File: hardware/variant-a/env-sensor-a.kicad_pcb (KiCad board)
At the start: 4 copper layers, 30 x 34 mm, 64 parts, among them J1 USB-C 16P, J2 Molex PicoBlade 3P, Q1 2N7002, SW1 SW_PROV, U1 ESP32-C6-MINI-1-N4, U2 SHT45-AD1F, U3 TPS62840DLC, U4 BQ24074RGTR, U5 USBLC6-2SC6

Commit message: build(boardgen): regenerate local charger programming layout
Regenerate both variants from the local C9/R12/R13 placement and routing correction. Fresh reports retain A42/B34 incomplete development connectivity and zero errors, warnings or parity differences; these generated boards are not fabrication approval.
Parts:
- moved R20 26.6 mm to (128.9, 88.0), turned to 90 degrees
- moved R12 19.8 mm to (121.5, 67.2)
- moved R13 19.2 mm to (121.5, 70.3), turned to 270 degrees
- moved R18 9.42 mm to (120.2, 87.0)
- turned C9 to 180 degrees
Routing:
- net BTN_PROV: track 131.5 -> 20.5 mm, vias 9 -> 0
- net EN: track 81.1 -> 6.70 mm, vias 5 -> 0
- net UART_RX: track 16.3 -> 78.9 mm, vias 1 -> 5
- net CHG_N: track 7.20 -> 56.8 mm, vias 2 -> 4
- net UART_TX: track 38.9 -> 0.00 mm, vias 3 -> 0
- net USB_EN2: track 29.9 -> 46.1 mm, vias 2 -> 5
- net LED_A: track 12.6 -> 0.00 mm, vias 2 -> 0
- net PACK_TS: track 27.3 -> 17.7 mm
- net ISET: track 0.00 -> 4.09 mm
- net ITERM: track 0.00 -> 3.99 mm
- net VBAT: track 15.3 -> 17.7 mm
- net GND: track 43.3 -> 45.4 mm, vias 20 -> 24
- net VBUS: track 11.3 -> 9.80 mm
- net ILIM: track 21.5 -> 22.3 mm

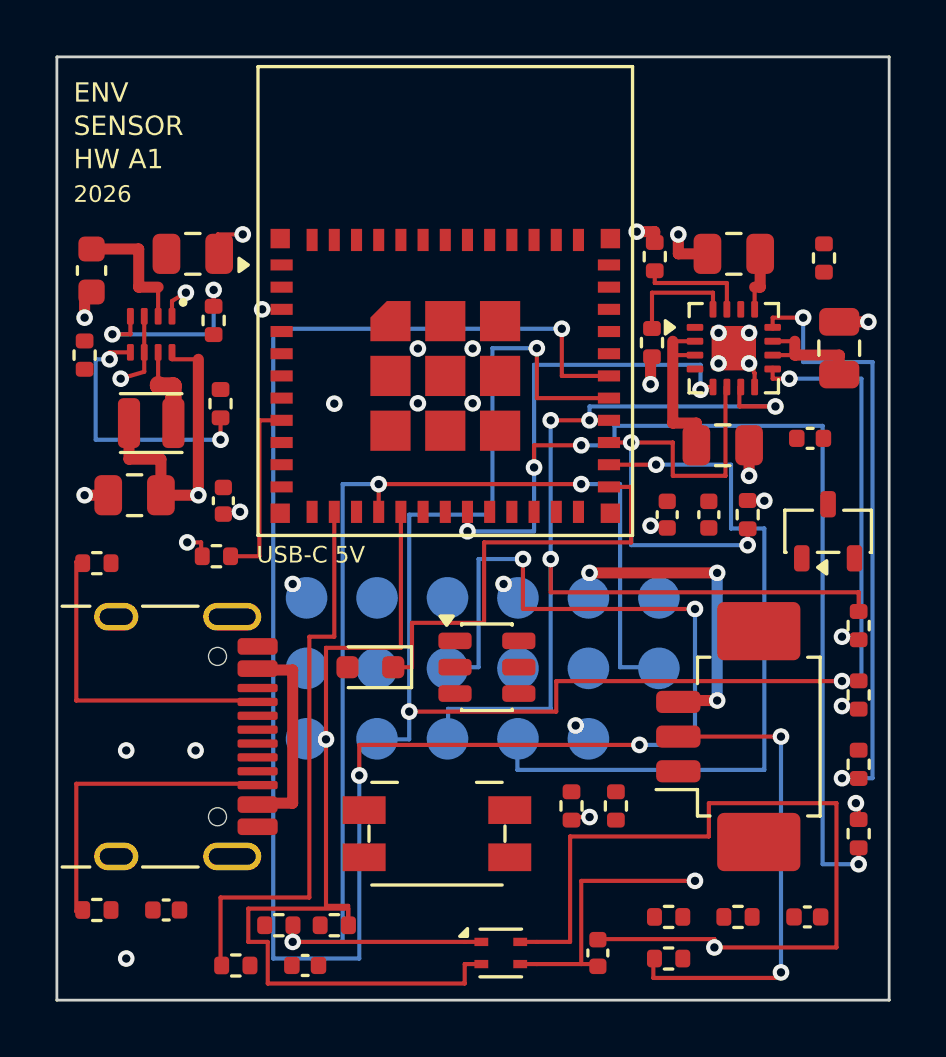
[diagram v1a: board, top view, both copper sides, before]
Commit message: build(boardgen): regenerate plane-connected body ground regions
Regenerate both layouts after adding explicit U1/C5/J2/U5 ground access. Fresh reports show no GND airwires, no errors/warnings/parity differences and A39/B35 total unfinished connections. Record exact development counts; fabrication remains blocked.
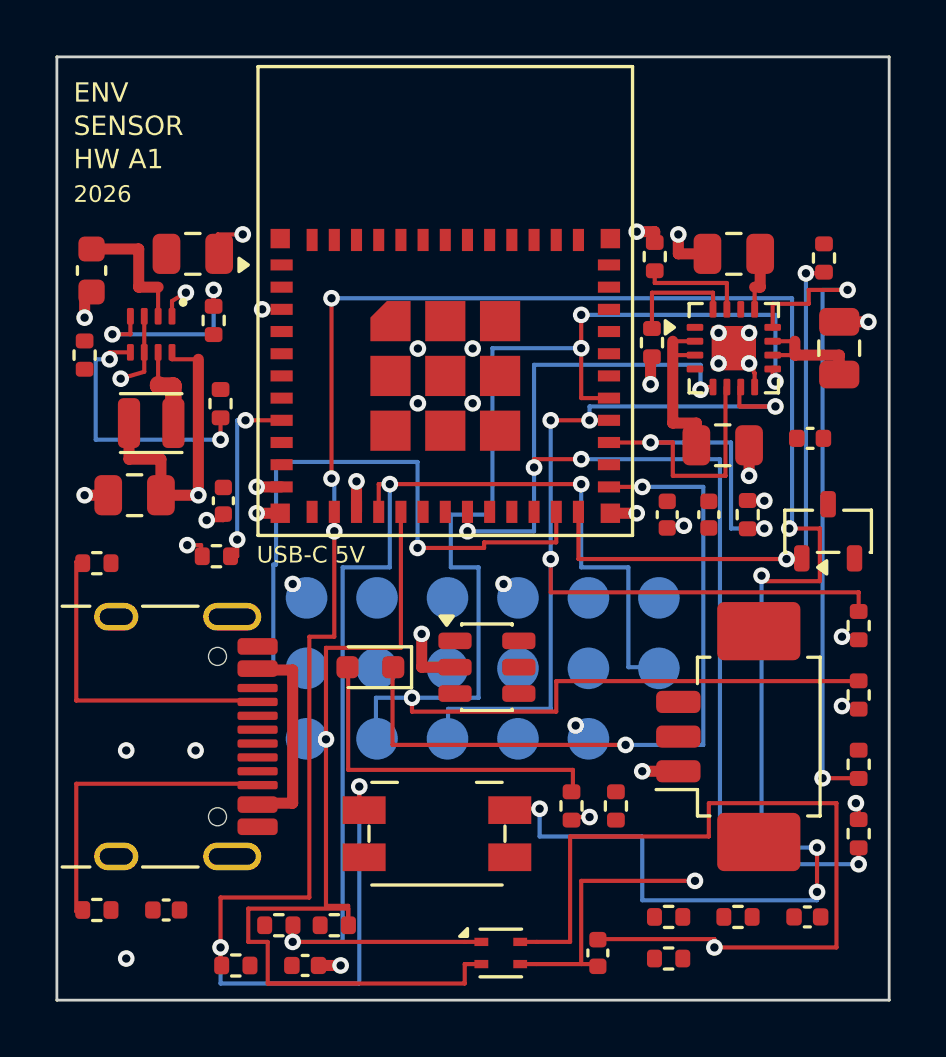
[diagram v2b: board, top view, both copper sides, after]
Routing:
- net BTN_PROV: track 20.5 -> 101.8 mm, vias 0 -> 10
- net UART_RX: track 78.9 -> 0.00 mm, vias 5 -> 0
- net TEST_MODE: track 26.6 -> 0.00 mm, vias 1 -> 0
- net BOOT_N: track 0.00 -> 23.2 mm, vias 0 -> 1
- net CHARGE_ENABLE: track 0.00 -> 21.3 mm, vias 0 -> 2
- net PACK_TS: track 17.7 -> 0.00 mm, vias 2 -> 0
- net LED_A: track 0.00 -> 12.6 mm
- net VBAT: track 17.7 -> 6.20 mm, vias 3 -> 0
- net LED_N: track 15.9 -> 26.7 mm, vias 0 -> 2
- net GND: track 45.4 -> 53.7 mm, vias 24 -> 30
- net USB_EN2: track 46.1 -> 43.7 mm
- net ILIM: track 22.3 -> 23.9 mm
- net CHG_N: track 56.8 -> 55.2 mm
- net USB_ISEL: track 17.1 -> 16.4 mm
- net EN: vias 0 -> 2

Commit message: build(boardgen): regenerate guarded USB layouts and fixture map
Regenerate both board layouts, design rules, fixture coordinates and mechanical placement inputs from the guarded USB generator. Fresh filled-board reports have zero errors, warnings and parity differences, with A31/B27 total unconnected items; neither USB data net nor GND has an airwire. Physical and fabrication qualification remain open.
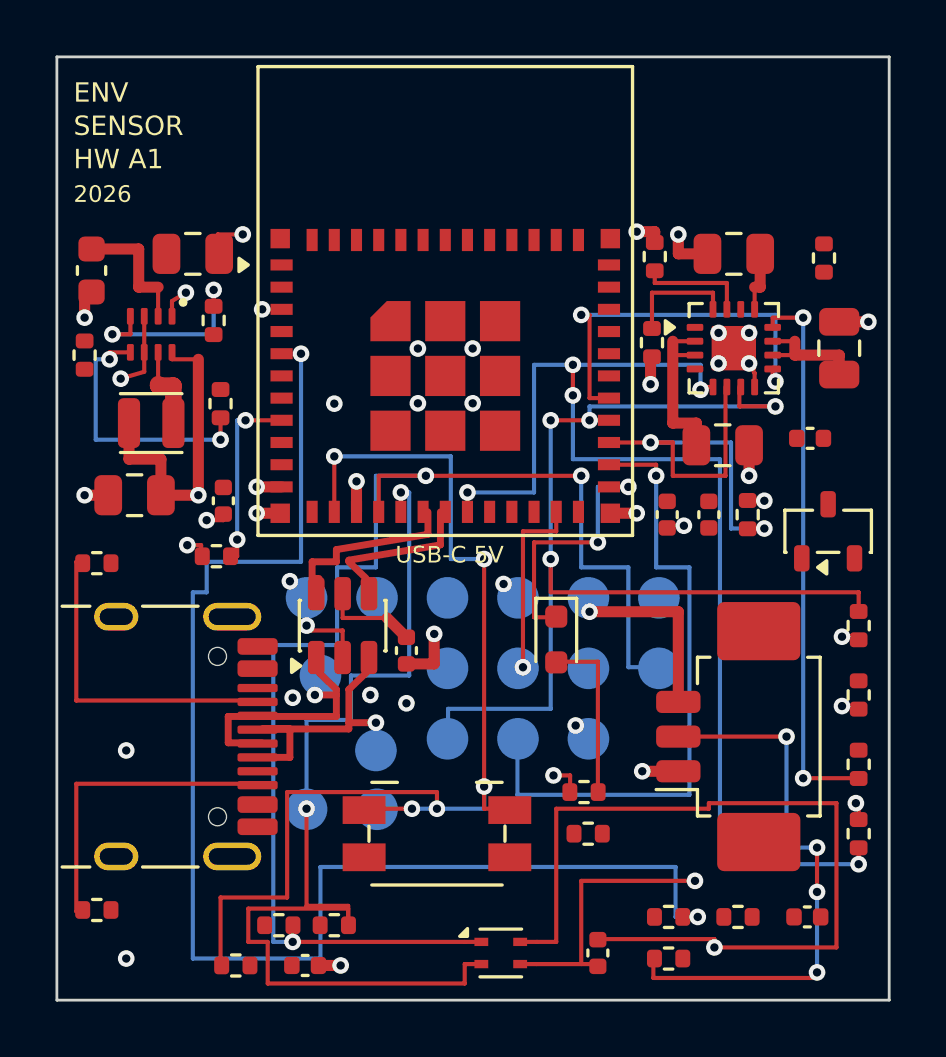
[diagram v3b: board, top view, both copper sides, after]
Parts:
- moved C14 12.7 mm to (112.6, 81.4), turned to 270 degrees
- moved TP11 9.66 mm to (109.5, 82.3)
- moved TP7 7.62 mm to (116.6, 82.0)
- moved TP8 7.62 mm to (119.2, 82.0)
- moved D1 6.77 mm to (118.0, 81.0), turned to 90 degrees
- moved TP10 5.91 mm to (111.5, 85.0)
- moved U5 5.41 mm to (110.3, 80.5), turned to 90 degrees
- moved TP13 2.54 mm to (109.0, 87.1)
- moved TP14 2.54 mm to (111.5, 87.1)
- moved R18 1.41 mm to (119.2, 88.0), turned to 0 degrees
- moved R2 0.67 mm to (119.0, 86.5), turned to 0 degrees
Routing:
- net BTN_PROV: track 101.8 -> 40.8 mm, vias 10 -> 5
- net VBAT_SENSE: track 0.00 -> 50.2 mm, vias 0 -> 2
- net CHG_N: track 55.2 -> 14.0 mm, vias 4 -> 2
- net TEST_MODE: track 0.00 -> 23.0 mm, vias 0 -> 1
- net CHARGE_ENABLE: track 21.3 -> 0.00 mm, vias 2 -> 0
- net PACK_TS: track 0.00 -> 20.3 mm, vias 0 -> 4
- net LED_N: track 26.7 -> 9.60 mm
- net BOOT_N: track 23.2 -> 6.80 mm
- net USB_D_P: track 0.00 -> 15.9 mm, vias 0 -> 1
- net USB_D_N: track 0.00 -> 15.7 mm, vias 0 -> 1
- net VBAT: track 6.20 -> 13.1 mm, vias 0 -> 1
- net LED_A: track 12.6 -> 6.20 mm
- net VBUS: track 9.80 -> 5.67 mm
- net ILIM: track 23.9 -> 20.1 mm
- net SDA: track 45.7 -> 49.3 mm
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- added copper zone on In2.Cu, net GND
